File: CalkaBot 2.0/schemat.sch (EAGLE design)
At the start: 55 parts, among them IC1 TB6612FNG, IC2 LM339D, IC3 7806DT, Q1 16MHz, X1 MINI-USB-32005-301

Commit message: niezapisane rzeczt
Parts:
- added U$3: (no value), untitled:GND
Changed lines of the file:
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@@
 <part name="P+3" library="supply1" library_urn="urn:adsk.eagle:library:371" deviceset="VCC" device=""/>
 <part name="GND2" library="supply1" library_urn="urn:adsk.eagle:library:371" deviceset="GND" device=""/>
-<part name="GND3" library="supply1" library_urn="urn:adsk.eagle:library:371" deviceset="GND" device=""/>
+<part name="GND3" library="supply1" library_urn="urn:adsk.eagle:library:371" deviceset="GND" device="">
+<attribute name="SPICEPREFIX" value="G"/>
+</part>
 <part name="R4" library="rcl" library_urn="urn:adsk.eagle:library:334" deviceset="R-EU_" device="R0805" package3d_urn="urn:adsk.eagle:package:23553/2" value="180R"/>
 <part name="P+4" library="supply1" library_urn="urn:adsk.eagle:library:371" deviceset="VCC" device=""/>
@@
 <part name="JP2" library="pinhead" library_urn="urn:adsk.eagle:library:325" deviceset="PINHD-1X5" device="" package3d_urn="urn:adsk.eagle:package:22469/2"/>
 <part name="JP3" library="pinhead" library_urn="urn:adsk.eagle:library:325" deviceset="PINHD-1X5" device="" package3d_urn="urn:adsk.eagle:package:22469/2"/>
+<part name="U$3" library="untitled" deviceset="GND" device=""/>
 </parts>
 <sheets>
@@
 <instance part="JP2" gate="A" x="-119.38" y="25.4" rot="R270"/>
 <instance part="JP3" gate="A" x="-119.38" y="15.24" rot="R270"/>
+<instance part="U$3" gate="G$1" x="-58.42" y="154.94"/>
 </instances>
 <busses>

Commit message: dodalem dipy
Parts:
- removed BUT1, BUT2, BUT3: (no value), switch-omron:10-XX
- removed JP3: (no value), pinhead:PINHD-1X5
- removed X1: MINI-USB-32005-301, con-cypressindustries:MINI-USB-32005-301
- added SW2: (no value), special:SW_DIP-3
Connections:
- removed net N$20: JP2.4, JP3.4, R26.1, X1.4
- new net N$11: JP2.4, R26.1
- net GND: now also SW2.4, SW2.5, SW2.6; no longer BUT1.S, BUT1.S1, BUT2.S, BUT2.S1, BUT3.S, BUT3.S1, JP3.1, JP3.2, X1.1, X1.2
- net MISO: now also SW2.3; no longer BUT1.P, BUT1.P1
- net MOSI: now also SW2.2; no longer BUT2.P, BUT2.P1
- net N$12: no longer JP3.3, X1.3
- net SCK: now also SW2.1; no longer BUT3.P, BUT3.P1
- net VBUS: no longer JP3.5, X1.5
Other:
- moved on the sheet: C10, R25, R26

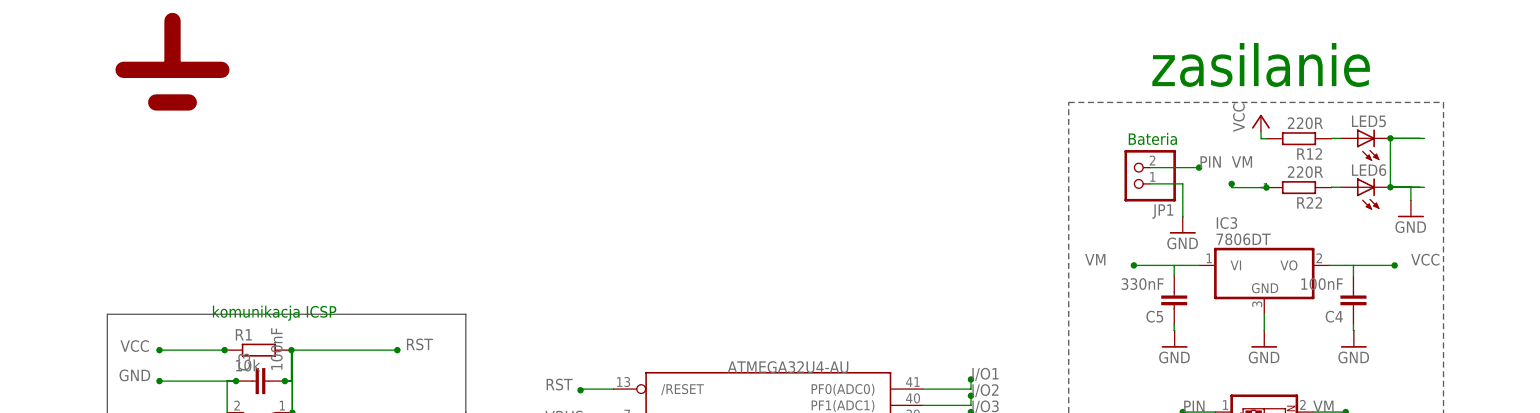
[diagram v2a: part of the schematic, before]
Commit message: dodano diode
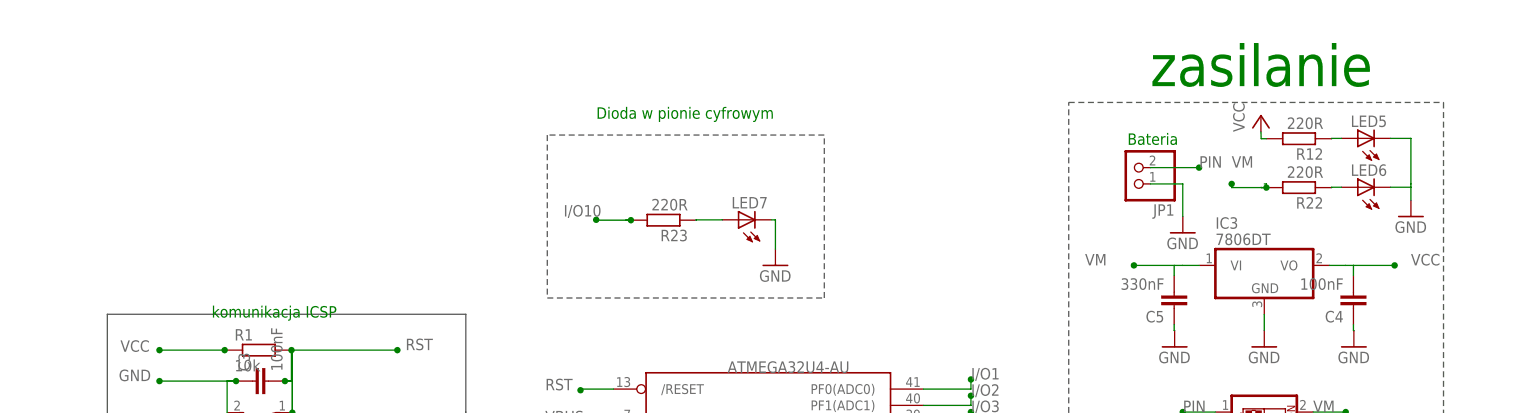
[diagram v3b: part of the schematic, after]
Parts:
- removed U$3: (no value), untitled:GND
- added LED7: (no value), led:LEDCHIP-LED0805
- added R23: 220R, rcl:R-EU_R0805
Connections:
- new net N$2: LED7.A, R23.1
- net GND: now also LED7.C
- net I/O10: now also R23.2
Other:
- note added: "Dioda w pionie cyfrowym"
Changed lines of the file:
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@@
 <part name="SW1" library="special" library_urn="urn:adsk.eagle:library:367" deviceset="SW_DIP-1" device="" package3d_urn="urn:adsk.eagle:package:26661/1"/>
 <part name="JP2" library="pinhead" library_urn="urn:adsk.eagle:library:325" deviceset="PINHD-1X5" device="" package3d_urn="urn:adsk.eagle:package:22469/2"/>
-<part name="U$3" library="untitled" deviceset="GND" device=""/>
 <part name="SW2" library="special" library_urn="urn:adsk.eagle:library:367" deviceset="SW_DIP-3" device="" package3d_urn="urn:adsk.eagle:package:26663/2"/>
 <part name="GND22" library="supply1" library_urn="urn:adsk.eagle:library:371" deviceset="GND" device=""/>
+<part name="R23" library="rcl" library_urn="urn:adsk.eagle:library:334" deviceset="R-EU_" device="R0805" package3d_urn="urn:adsk.eagle:package:23553/2" value="220R"/>
+<part name="LED7" library="led" library_urn="urn:adsk.eagle:library:259" deviceset="LED" device="CHIP-LED0805" package3d_urn="urn:adsk.eagle:package:15818/2"/>
+<part name="GND23" library="supply1" library_urn="urn:adsk.eagle:library:371" deviceset="GND" device=""/>
 </parts>
 <sheets>
@@
 <text x="47.244" y="143.256" size="1.778" layer="91">Bateria</text>
 <text x="50.8" y="152.4" size="6.4516" layer="91">zasilanie</text>
+<text x="-35.56" y="147.32" size="1.778" layer="91">Dioda w pionie cyfrowym</text>
 </plain>
 <instances>
@@
 <attribute name="VALUE" x="-129.54" y="31.75" size="1.778" layer="96" rot="R270"/>
 </instance>
-<instance part="U$3" gate="G$1" x="-58.42" y="154.94" smashed="yes"/>
 <instance part="SW2" gate="A" x="-22.86" y="-20.32" smashed="yes" rot="R90">
 <attribute name="NAME" x="-28.575" y="-25.4" size="1.778" layer="95" rot="R90"/>
@@
 <instance part="GND22" gate="1" x="-22.86" y="-33.02" smashed="yes">
 <attribute name="VALUE" x="-25.4" y="-35.56" size="1.778" layer="96"/>
+</instance>
+<instance part="R23" gate="G$1" x="-25.062" y="131.508" smashed="yes" rot="R180">
+<attribute name="NAME" x="-21.252" y="130.0094" size="1.778" layer="95" rot="R180"/>
+<attribute name="VALUE" x="-21.252" y="134.81" size="1.778" layer="96" rot="R180"/>
+</instance>
+<instance part="LED7" gate="G$1" x="-13.36" y="131.56" smashed="yes" rot="R90">
+<attribute name="NAME" x="-8.788" y="135.116" size="1.778" layer="95" rot="R180"/>
+<attribute name="VALUE" x="-8.788" y="137.275" size="1.778" layer="96" rot="R180"/>
+</instance>
+<instance part="GND23" gate="1" x="-7.62" y="124.46" smashed="yes">
+<attribute name="VALUE" x="-10.16" y="121.92" size="1.778" layer="96"/>
 </instance>
 </instances>
@@
 <wire x1="96.52" y1="93.98" x2="38.1" y2="93.98" width="0.762" layer="92" style="shortdash"/>
 <wire x1="38.1" y1="93.98" x2="38.1" y2="149.86" width="0.762" layer="92" style="shortdash"/>
+</segment>
+</bus>
+<bus name="B$7">
+<segment>
+<wire x1="-43.18" y1="144.78" x2="-43.18" y2="119.38" width="0.762" layer="92" style="shortdash"/>
+<wire x1="-43.18" y1="119.38" x2="0" y2="119.38" width="0.762" layer="92" style="shortdash"/>
+<wire x1="0" y1="119.38" x2="0" y2="144.78" width="0.762" layer="92" style="shortdash"/>
+<wire x1="0" y1="144.78" x2="-43.18" y2="144.78" width="0.762" layer="92" style="shortdash"/>
 </segment>
 </bus>
@@
 </segment>
 <segment>
-<pinref part="LED5" gate="G$1" pin="C"/>
-<wire x1="88.24" y1="144.26" x2="92.86" y2="144.26" width="0.1524" layer="91"/>
-<wire x1="88.24" y1="144.26" x2="93.56" y2="144.26" width="0.1524" layer="91"/>
-<junction x="88.24" y="144.26"/>
-<wire x1="88.24" y1="144.26" x2="88.24" y2="136.64" width="0.1524" layer="91"/>
-<pinref part="GND19" gate="1" pin="GND"/>
-<wire x1="88.24" y1="136.64" x2="91.44" y2="136.64" width="0.1524" layer="91"/>
-<wire x1="91.44" y1="136.64" x2="91.44" y2="134.62" width="0.1524" layer="91"/>
-<pinref part="LED6" gate="G$1" pin="C"/>
-<wire x1="88.24" y1="136.64" x2="92.86" y2="136.64" width="0.1524" layer="91"/>
-<wire x1="88.24" y1="136.64" x2="93.56" y2="136.64" width="0.1524" layer="91"/>
-<junction x="88.24" y="136.64"/>
-</segment>
-<segment>
 <pinref part="IC1" gate="G$1" pin="PGND2"/>
 <wire x1="68.58" y1="53.84" x2="68.58" y2="51.3" width="0.1524" layer="91"/>
@@
 <pinref part="C10" gate="G$1" pin="-"/>
 <wire x1="-104.14" y1="48.26" x2="-104.14" y2="38.1" width="0.1524" layer="91"/>
+</segment>
+<segment>
+<pinref part="LED5" gate="G$1" pin="C"/>
+<pinref part="LED6" gate="G$1" pin="C"/>
+<wire x1="91.44" y1="144.26" x2="91.44" y2="137.16" width="0.1524" layer="91"/>
+<wire x1="91.44" y1="137.16" x2="91.44" y2="136.64" width="0.1524" layer="91"/>
+<wire x1="88.24" y1="136.64" x2="91.44" y2="136.64" width="0.1524" layer="91"/>
+<wire x1="88.24" y1="144.26" x2="91.44" y2="144.26" width="0.1524" layer="91"/>
+<pinref part="GND19" gate="1" pin="GND"/>
+<wire x1="91.44" y1="136.64" x2="91.44" y2="134.62" width="0.1524" layer="91"/>
+</segment>
+<segment>
+<pinref part="LED7" gate="G$1" pin="C"/>
+<pinref part="GND23" gate="1" pin="GND"/>
+<wire x1="-8.28" y1="131.56" x2="-7.62" y2="131.56" width="0.1524" layer="91"/>
+<wire x1="-7.62" y1="131.56" x2="-7.62" y2="127" width="0.1524" layer="91"/>
 </segment>
 </net>
@@
 <label x="25.4" y="88.9" size="1.778" layer="95"/>
 </segment>
+<segment>
+<pinref part="R23" gate="G$1" pin="2"/>
+<wire x1="-31" y1="131.508" x2="-30.142" y2="131.508" width="0.1524" layer="91"/>
+<wire x1="-30.142" y1="131.508" x2="-35.56" y2="131.508" width="0.1524" layer="91"/>
+<wire x1="-35.56" y1="131.508" x2="-35.56" y2="131.572" width="0.1524" layer="91"/>
+<junction x="-30.142" y="131.508"/>
+<junction x="-35.56" y="131.572"/>
+<label x="-40.64" y="132.08" size="1.778" layer="95"/>
+</segment>
 </net>
 <net name="PIN" class="0">
@@
 </segment>
 </net>
+<net name="N$2" class="0">
+<segment>
+<pinref part="R23" gate="G$1" pin="1"/>
+<pinref part="LED7" gate="G$1" pin="A"/>
+<wire x1="-19.982" y1="131.508" x2="-19.982" y2="131.56" width="0.1524" layer="91"/>
+<wire x1="-19.982" y1="131.56" x2="-15.9" y2="131.56" width="0.1524" layer="91"/>
+</segment>
+</net>
